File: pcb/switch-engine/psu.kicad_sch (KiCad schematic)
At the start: 122 parts, among them J1 CONN_PCIE_PWR_8PIN, J2 CONN_IBC_MGMT, J3 CONN_01X03, J4 CORTEX_DEBUG_ETM, J5 FAN_01, J6 FAN_01, SW1 SWITCH, SW2 SWITCH, U1 STM32L431-QFN48, U2 MYMGK1R812ERSR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

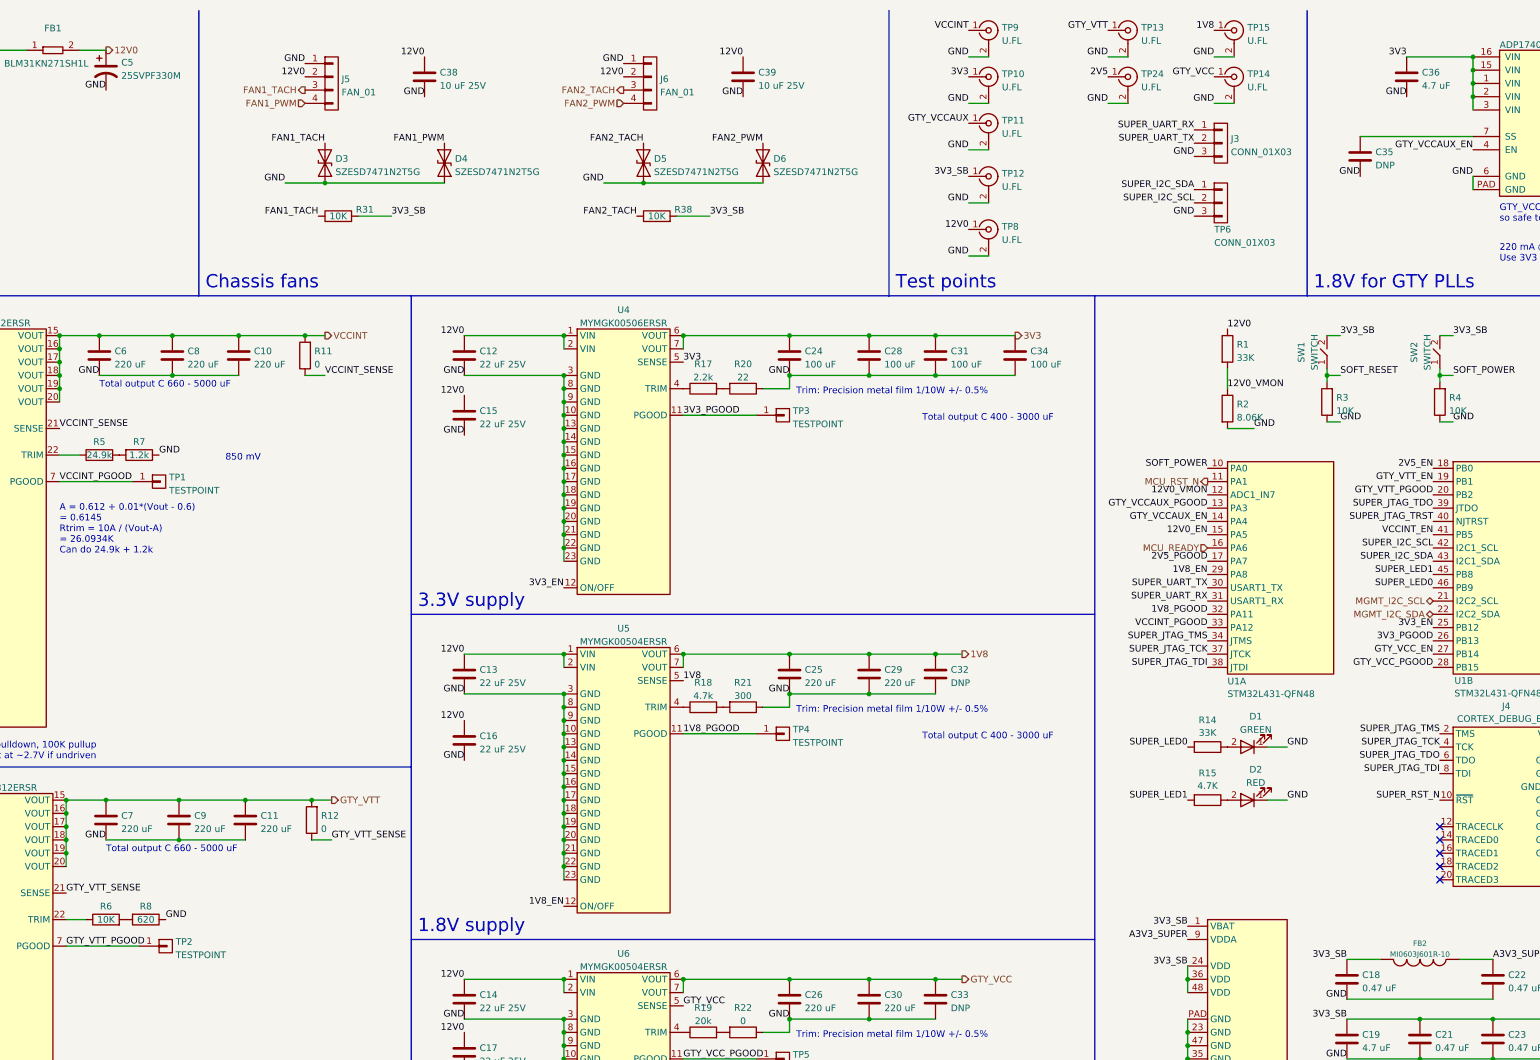
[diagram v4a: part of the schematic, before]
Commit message: Continued SERDES SI tuning
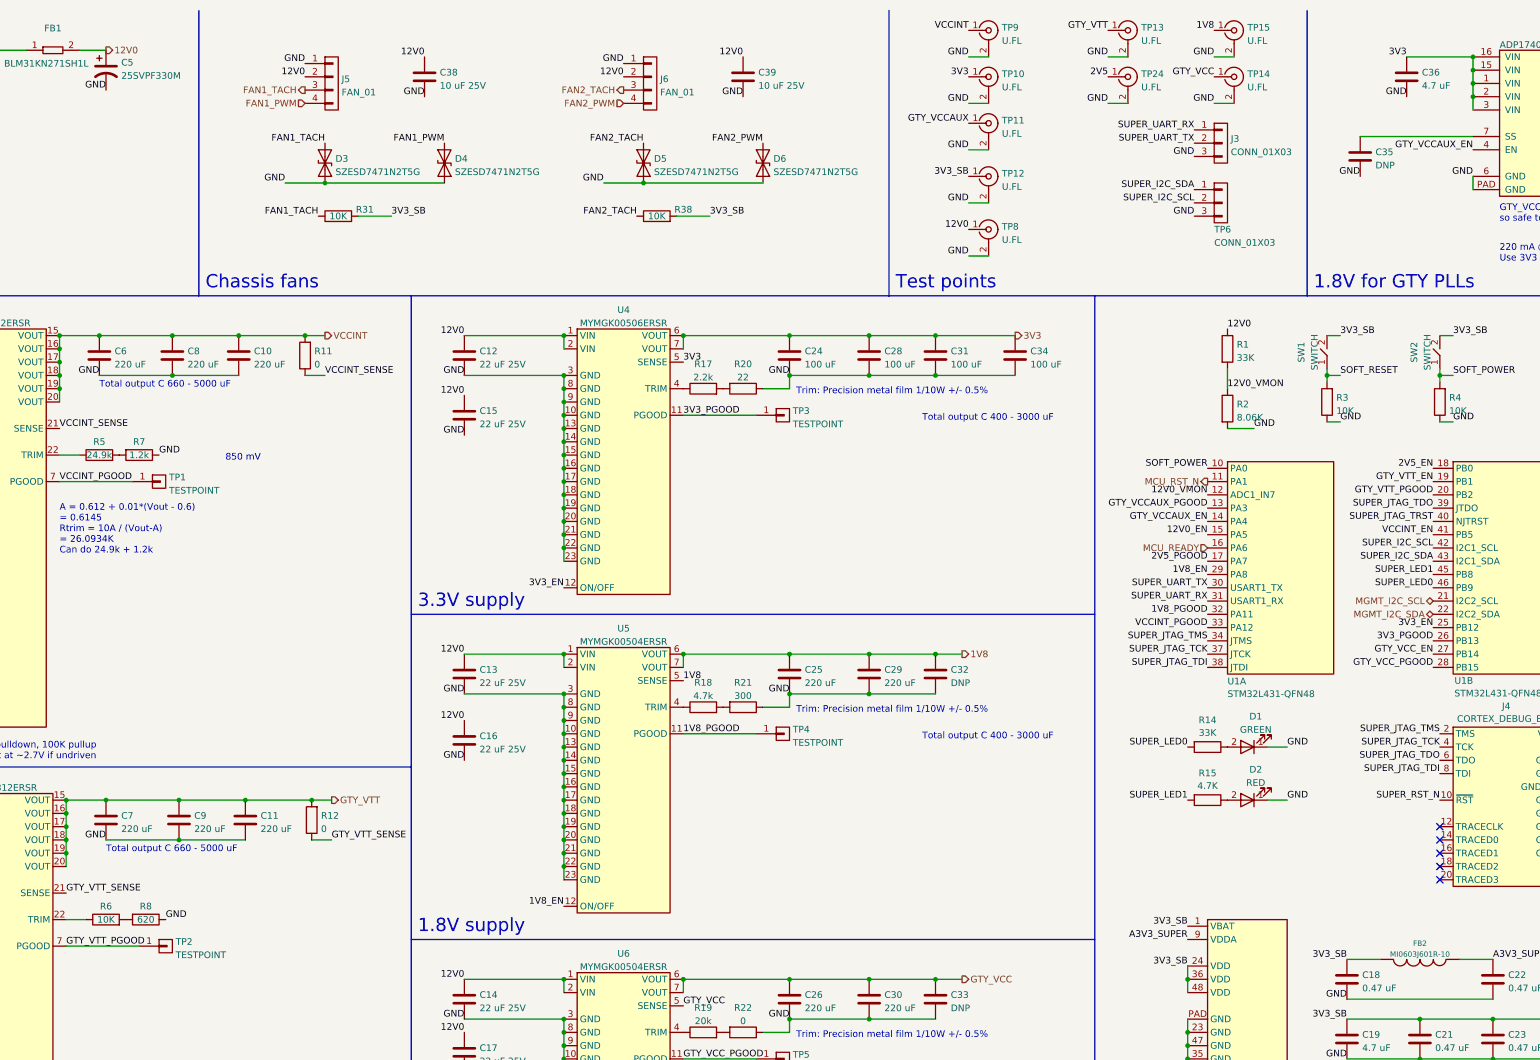
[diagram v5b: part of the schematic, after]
